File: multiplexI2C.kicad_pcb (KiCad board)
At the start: 2 copper layers, 48.3 x 71.1 mm, 59 parts, among them J1 Screw_Terminal_01x04, J17 Conn_01x04_Pin, J18 PinSocket_1x20_P2.54mm_Vertic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, J19 PinSocket_1x20_P2.54mm_Vertic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, J2 Screw_Terminal_01x04, J20 Screw_Terminal_01x02, J3 Screw_Terminal_01x04, J4 Screw_Terminal_01x04, J5 Screw_Terminal_01x04, J6 Screw_Terminal_01x04, J7 Screw_Terminal_01x04, J8 Screw_Terminal_01x04, J9 header_0.25sqmm_1x04_P4.2mm_D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, U1 TCA9548A, U2 RFM95W-915S2

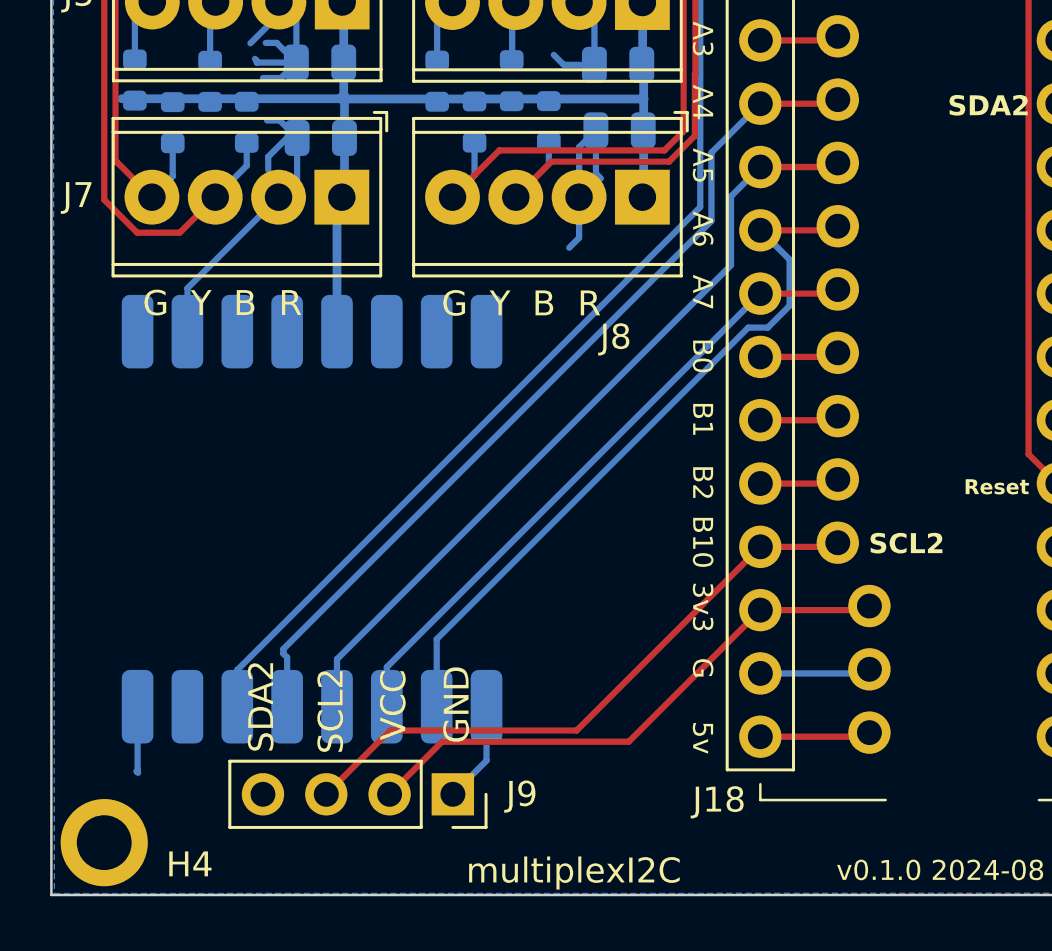
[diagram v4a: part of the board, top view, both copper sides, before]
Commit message: added fill zone behind radio and other cleanup.
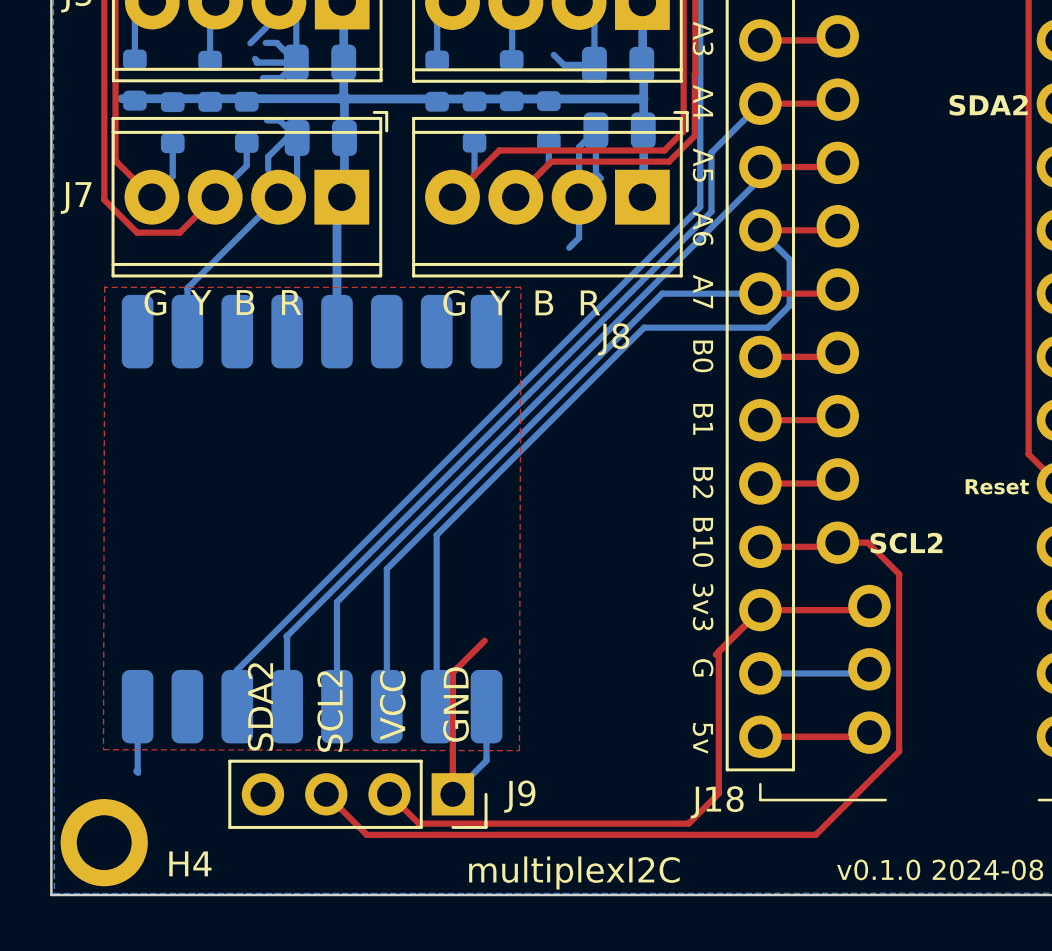
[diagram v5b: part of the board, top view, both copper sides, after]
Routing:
- net /SCL2: track 24.7 -> 38.3 mm
- net Net-(J18-3v3): track 22.2 -> 29.0 mm
- net GND: track 66.0 -> 72.7 mm
- net MISO: track 29.0 -> 31.4 mm
- net MOSI: track 25.8 -> 28.1 mm
- added copper zone on F.Cu, net GND
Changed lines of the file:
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@@
+	)
+	(segment
+		(start 65.64 86.33)
+		(end 66.92 85.05)
+		(width 0.25)
+		(layer "F.Cu")
+		(net 2)
 	)
 	(segment
@@
 		(start 53.705 54.01)
 		(end 52.48 54.01)
+		(width 0.25)
+		(layer "F.Cu")
+		(net 2)
+	)
+	(segment
+		(start 65.64 91.21)
+		(end 65.64 86.33)
 		(width 0.25)
 		(layer "F.Cu")
@@
 	)
 	(segment
-		(start 70.608 88.65)
-		(end 63.12 88.65)
+		(start 82.287081 81.115)
+		(end 83.55 82.377919)
 		(width 0.25)
 		(layer "F.Cu")
@@
 	)
 	(segment
-		(start 77.978 81.28)
-		(end 70.608 88.65)
+		(start 81.085 81.115)
+		(end 82.287081 81.115)
 		(width 0.25)
 		(layer "F.Cu")
@@
 	)
 	(segment
-		(start 63.12 88.65)
+		(start 83.55 89.49)
+		(end 80.205 92.835)
+		(width 0.25)
+		(layer "F.Cu")
+		(net 5)
+	)
+	(segment
+		(start 83.55 82.377919)
+		(end 83.55 89.49)
+		(width 0.25)
+		(layer "F.Cu")
+		(net 5)
+	)
+	(segment
+		(start 62.185 92.835)
 		(end 60.56 91.21)
+		(width 0.25)
+		(layer "F.Cu")
+		(net 5)
+	)
+	(segment
+		(start 80.205 92.835)
+		(end 62.185 92.835)
 		(width 0.25)
 		(layer "F.Cu")
@@
 	)
 	(segment
-		(start 65.21 89.1)
-		(end 63.1 91.21)
+		(start 76.31 85.488)
+		(end 76.31 91.18)
 		(width 0.25)
 		(layer "F.Cu")
@@
 	)
 	(segment
-		(start 72.698 89.1)
-		(end 65.21 89.1)
+		(start 77.978 83.82)
+		(end 76.31 85.488)
 		(width 0.25)
 		(layer "F.Cu")
@@
 	(segment
 		(start 77.978 83.82)
-		(end 72.698 89.1)
+		(end 76.19 85.608)
+		(width 0.25)
+		(layer "F.Cu")
+		(net 7)
+	)
+	(segment
+		(start 76.31 91.18)
+		(end 75.105 92.385)
+		(width 0.25)
+		(layer "F.Cu")
+		(net 7)
+	)
+	(segment
+		(start 75.105 92.385)
+		(end 64.275 92.385)
+		(width 0.25)
+		(layer "F.Cu")
+		(net 7)
+	)
+	(segment
+		(start 64.275 92.385)
+		(end 63.1 91.21)
 		(width 0.25)
 		(layer "F.Cu")
@@
 	)
 	(segment
+		(start 62.99 82.17)
+		(end 62.99 87.695)
+		(width 0.25)
+		(layer "B.Cu")
+		(net 15)
+	)
+	(segment
+		(start 74.04 71.12)
+		(end 62.99 82.17)
+		(width 0.25)
+		(layer "B.Cu")
+		(net 15)
+	)
+	(segment
 		(start 77.978 71.12)
-		(end 62.99 86.108)
-		(width 0.25)
-		(layer "B.Cu")
-		(net 15)
-	)
-	(segment
-		(start 62.99 86.108)
-		(end 62.99 87.695)
+		(end 74.04 71.12)
 		(width 0.25)
 		(layer "B.Cu")
@@
 	)
 	(segment
-		(start 76.015 68.205)
-		(end 58.84 85.38)
-		(width 0.25)
-		(layer "B.Cu")
-		(net 20)
-	)
-	(segment
-		(start 58.84 85.38)
-		(end 58.84 85.57)
-		(width 0.25)
-		(layer "B.Cu")
-		(net 20)
-	)
-	(segment
-		(start 76.015 65.463)
-		(end 76.015 68.205)
-		(width 0.25)
-		(layer "B.Cu")
-		(net 20)
-	)
-	(segment
 		(start 77.978 63.5)
 		(end 76.015 65.463)
@@
 	)
 	(segment
-		(start 58.99 85.72)
+		(start 58.99 84.9)
 		(end 58.99 87.695)
 		(width 0.25)
@@
 	)
 	(segment
-		(start 58.84 85.57)
-		(end 58.99 85.72)
+		(start 76.015 67.831396)
+		(end 58.968198 84.878198)
+		(width 0.25)
+		(layer "B.Cu")
+		(net 20)
+	)
+	(segment
+		(start 58.968198 84.878198)
+		(end 58.99 84.9)
+		(width 0.25)
+		(layer "B.Cu")
+		(net 20)
+	)
+	(segment
+		(start 76.015 65.463)
+		(end 76.015 67.831396)
 		(width 0.25)
 		(layer "B.Cu")
@@
 	)
 	(segment
-		(start 60.99 85.79)
+		(start 60.99 83.492792)
 		(end 60.99 87.695)
 		(width 0.25)
@@
 	)
 	(segment
+		(start 77.978 66.504792)
+		(end 60.99 83.492792)
+		(width 0.25)
+		(layer "B.Cu")
+		(net 21)
+	)
+	(segment
 		(start 77.978 66.04)
-		(end 76.803 67.215)
-		(width 0.25)
-		(layer "B.Cu")
-		(net 21)
-	)
-	(segment
-		(start 76.803 67.215)
-		(end 76.803 69.977)
-		(width 0.25)
-		(layer "B.Cu")
-		(net 21)
-	)
-	(segment
-		(start 76.803 69.977)
-		(end 60.99 85.79)
+		(end 77.978 66.504792)
 		(width 0.25)
 		(layer "B.Cu")
@@
 	)
 	(segment
-		(start 64.99 84.986299)
+		(start 64.99 80.806396)
 		(end 64.99 87.695)
 		(width 0.25)
@@
 	)
 	(segment
-		(start 77.491299 72.485)
-		(end 64.99 84.986299)
+		(start 73.311396 72.485)
+		(end 64.99 80.806396)
 		(width 0.25)
 		(layer "B.Cu")
@@
 	)
 	(segment
+		(start 77.978 68.58)
+		(end 79.153 69.755)
+		(width 0.25)
+		(layer "B.Cu")
+		(net 22)
+	)
+	(segment
 		(start 78.274701 72.485)
-		(end 77.491299 72.485)
+		(end 73.311396 72.485)
 		(width 0.25)
 		(layer "B.Cu")
@@
 		(start 79.153 71.606701)
 		(end 78.274701 72.485)
-		(width 0.25)
-		(layer "B.Cu")
-		(net 22)
-	)
-	(segment
-		(start 77.978 68.58)
-		(end 79.153 69.755)
 		(width 0.25)
 		(layer "B.Cu")
@@
 	)
 	(zone
+		(net 2)
+		(net_name "GND")
+		(layer "F.Cu")
+		(hatch edge 0.5)
+		(priority 1)
+		(connect_pads
+			(clearance 0.29)
+		)
+		(min_thickness 0.25)
+		(filled_areas_thickness no)
+		(fill yes
+			(thermal_gap 0.5)
+			(thermal_bridge_width 0.5)
+		)
+		(polygon
+			(pts
+				(xy 51.67 70.84) (xy 51.62 89.42) (xy 68.31 89.46) (xy 68.37 70.87) (xy 51.69 70.87) (xy 51.66 70.89)
+			)
+		)
+	)
+	(zone

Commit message: some cleanup. About to split two lra module branches.
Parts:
- moved J9 1.62 mm to (65.6, 92.8)
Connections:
- net DI0 renamed /RFM95W/DI0
- net DI1 renamed /RFM95W/DI1
- net Net-(J19-B4) renamed DIO0
- net Net-(J19-B5) renamed DIO1
- J9 pad 4: unconnected-(J9-SDA-Pad4) -> /SDA2
- U2 pad 11: DI3 -> unconnected-(U2-DIO3-Pad11)
- U2 pad 12: DI4 -> unconnected-(U2-DIO4-Pad12)
- U2 pad 16: DI2 -> unconnected-(U2-DIO2-Pad16)
- U2 pad 7: DI5 -> unconnected-(U2-DIO5-Pad7)
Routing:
- net /SDA2: track 2.54 -> 69.7 mm
- net /RFM95W/DI0: track 0.00 -> 37.6 mm, vias 0 -> 2
- net /RFM95W/DI1: track 0.00 -> 34.7 mm, vias 0 -> 2
- net RESET: track 46.1 -> 66.6 mm
- net NSS: track 35.1 -> 48.5 mm
- net GND: track 72.7 -> 61.9 mm
- net SCK: track 31.7 -> 41.8 mm
- net MOSI: track 28.1 -> 32.4 mm
- net MISO: track 31.4 -> 32.5 mm
- net /SCL2: track 38.3 -> 39.0 mm
- net Net-(J18-3v3): track 29.0 -> 29.7 mm
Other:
- board text added: "MISO"
- board text added: "MOSI"
- board text added: "NSS"
- board text added: "SCK"
- board text added: "SPI Reset"
